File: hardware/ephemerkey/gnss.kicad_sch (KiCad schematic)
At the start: 0 parts

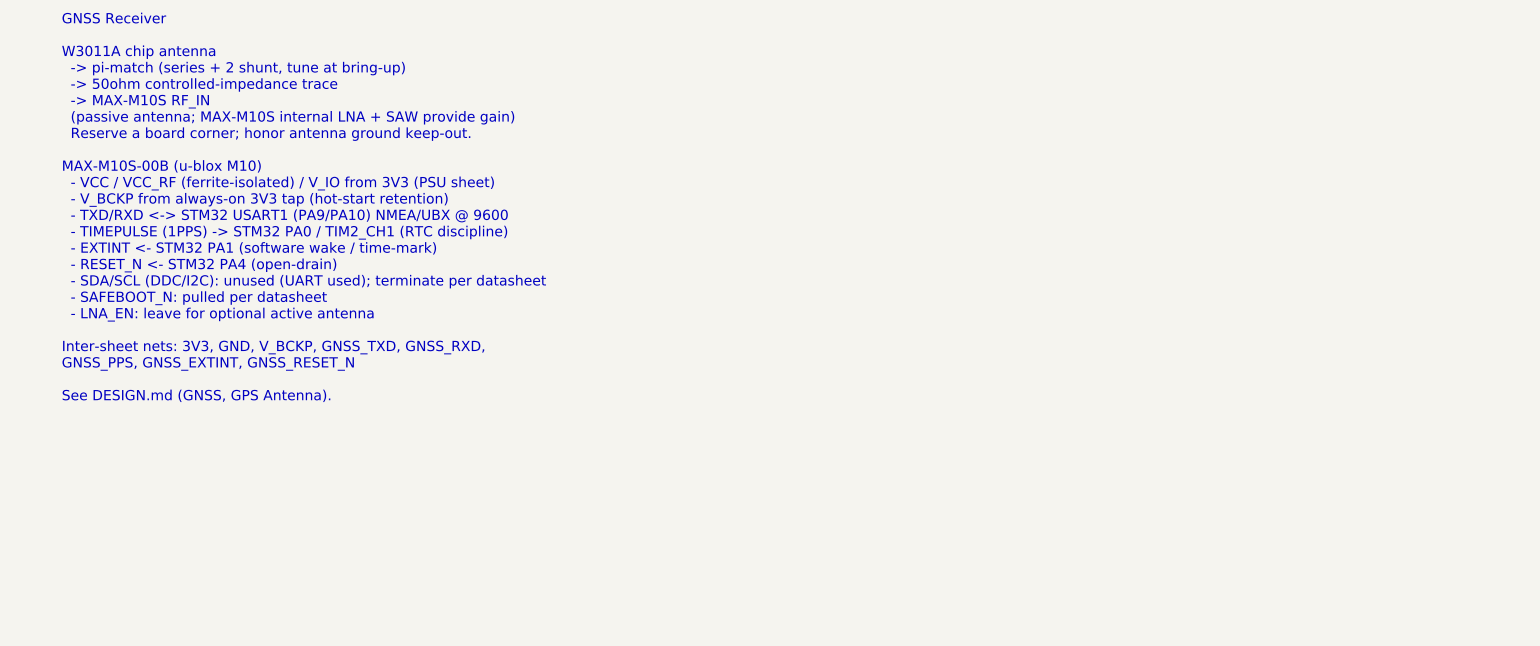
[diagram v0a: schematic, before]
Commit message: Populate schematic sheets per subsystem (placed, not wired)
Adopt the house schgen workflow (kschgen.py + manifest), matching notchdeck/
tsumikoro: schematic is GENERATED from scripts/ephemerkey.schgen.py, parts
PLACED with per-sheet on-canvas wiring notes; wiring is the next eeschema phase.

57 components across MCU / PSU / GNSS / Sensors, every line on a real KiCad
bundled symbol+footprint and a JLCPCB LCSC (0402 passives, 0805 bulk):
- MCU: STM32U083KCU6, 32.768kHz LSE crystal (C32346) + 12pF loads, SWD TC2030,
  lock-out header, decoupling, BOOT0/NRST, button, status LEDs.
- PSU: USB-C (GCT USB4105) + USBLC6 ESD + 5.1k CC, MCP73831 charger (Rprog 4.7k
  ~213mA for 500mAh), AO3401A load-share + B5819W, TPS63900 + FNR3015 2.2µH
  (small) + 10µF caps, JST-PH RA battery (S2B-PH-K-S).
- GNSS: MAX-M10S + W3011A + pi-match (series 0R, shunts DNP), VCC_RF ferrite,
  V_BCKP/V_IO/VCC decoupling.
- Sensors: LIS3DH + decoupling + 4.7k I2C pull-ups.

Tooling: kschgen.py, kicad-sch-check.py, kicad-sch-render.sh; Makefile gen/
check/render targets. make check: 57 comps, 57/57 footprints, no dup refs.
Added hardware/PARTS.md (BOM source of truth). CLAUDE.md documents the workflow.

Co-Authored-By: Claude Opus 4.8 (1M context) <noreply@anthropic.com>
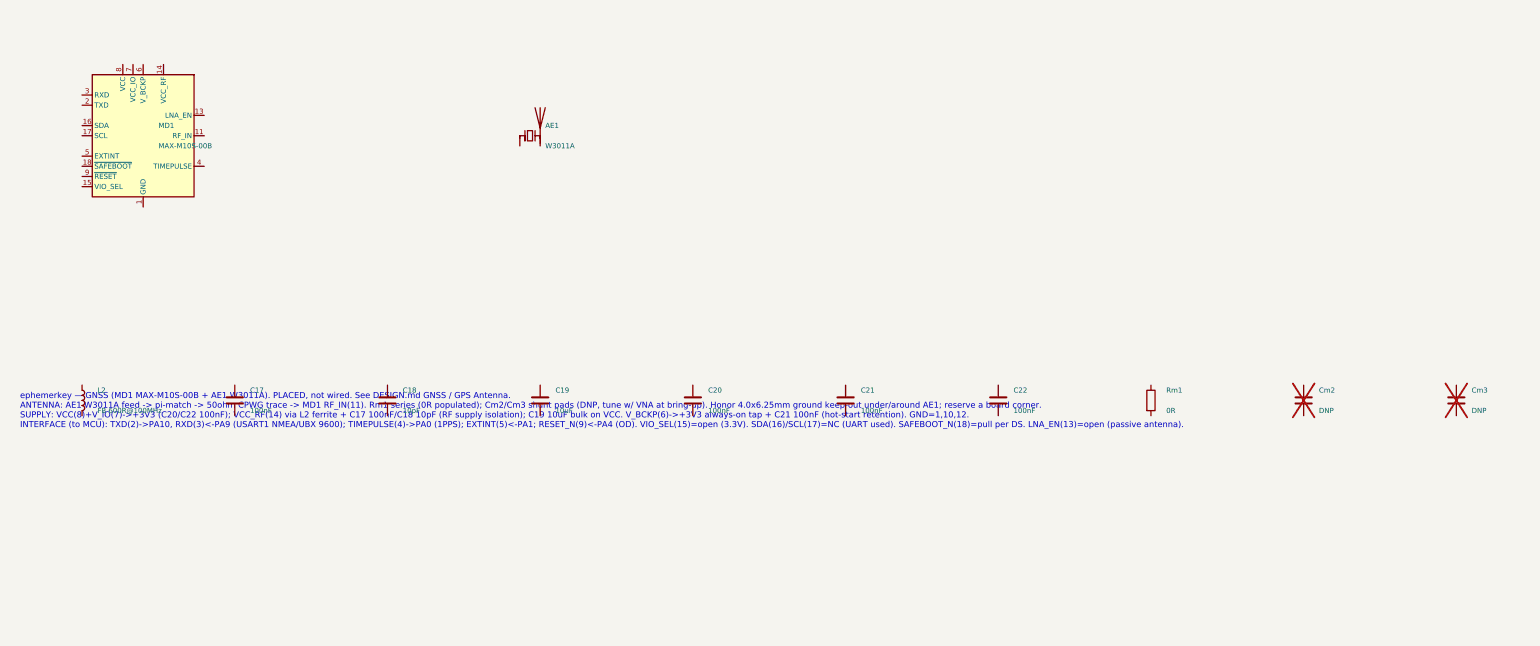
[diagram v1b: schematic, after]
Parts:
- added AE1: W3011A, RF_Antenna:Pulse_W3011, symbol Device:Antenna_Chip
- added C17, C20, C21, C22: 100nF, Capacitor_SMD:C_0402_1005Metric, symbol Device:C
- added C18: 10pF, Capacitor_SMD:C_0402_1005Metric, symbol Device:C
- added C19: 10uF, Capacitor_SMD:C_0805_2012Metric, symbol Device:C
- added Cm2, Cm3: DNP, Capacitor_SMD:C_0402_1005Metric, symbol Device:C
- added L2: FB 600R@100MHz, Inductor_SMD:L_0402_1005Metric, symbol Device:L
- added MD1: MAX-M10S-00B, RF_GPS:ublox_MAX, symbol RF_GPS:MAX-M10S
- added Rm1: 0R, Resistor_SMD:R_0402_1005Metric, symbol Device:R
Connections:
- new net: MD1.1 (GND), MD1.10 (GND), MD1.12 (GND)
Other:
- note added: "ephemerkey — GNSS (MD1 MAX-M10S-00B + AE1 W3011A). PLACED, not wired. See DESIGN.md GNSS / GPS Antenna. ANTENNA: AE1 W3011A feed -> pi-match -> 50ohm CPWG trace -> MD1 RF_IN(11). Rm1 series (0R populated); Cm2/Cm3 shunt pads (DNP, tune w/ VNA at bring-up). Honor 4.0x6.25mm ground keep-out under/around AE1; reserve a board corner. SUPPLY: VCC(8)+V_IO(7)->+3V3 (C20/C22 100nF); VCC_RF(14) via L2 fer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"
- note removed: "GNSS Receiver W3011A chip antenna -> pi-match (series + 2 shunt, tune at bring-up) -> 50ohm controlled-impedance trace -> MAX-M10S RF_IN (passive antenna; MAX-M10S internal LNA + SAW provide gain) Reserve a board corner; honor antenna ground keep-out. MAX-M10S-00B (u-blox M10) - VCC / VCC_RF (ferrite-isolated) / V_IO from 3V3 (PSU sheet) - V_BCKP from always-on 3V3 tap (hot-start retention) - TXD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"
- company: (none) -> EphemerKey Authors
- title: ephemerkey — GNSS -> ephemerkey — GNSS (MAX-M10S + antenna)

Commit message: Pinout-guide notes; vendor MAX + switch 3D models; 3 user buttons + DFU
Wiring notes: rewrote the four sheet notes from run-on prose into per-pin
PINOUT GUIDES (pin → net/function tables) per request.

3D models:
- MAX-M10S: vendored ublox_MAX-M10S.step (u-blox MAX form-factor, AP214, from
  fcmadwar/3D-Step-Models-Library) + project footprint ephemerkey:ublox_MAX
  with (model) repointed. Verify offset/rotation in 3D viewer.
- Switches: reuse tsumikoro's vendored ephemerkey:SW_Push_1P1T_XKB_TS-1187A
  footprint + STEP (the XKB TS-1187A model isn't in this KiCad bundle).
- Remaining to download: STM32U083 (UFQFPN-32), W3011A.

Switches: 3 user buttons (SW1→PA5, SW2→PA15 active-low; SW3→PF3/BOOT0
active-high). Holding SW3 at reset enters the STM32U0 ROM bootloader → USB DFU
over USB-C (confirmed in AN2606; crystal-less USB via HSI48+CRS).

make check: 59 components, 59/59 footprints, no dup refs. DESIGN.md pin budget +
library map, PARTS.md, 3dmodels README updated.

Co-Authored-By: Claude Opus 4.8 (1M context) <noreply@anthropic.com>
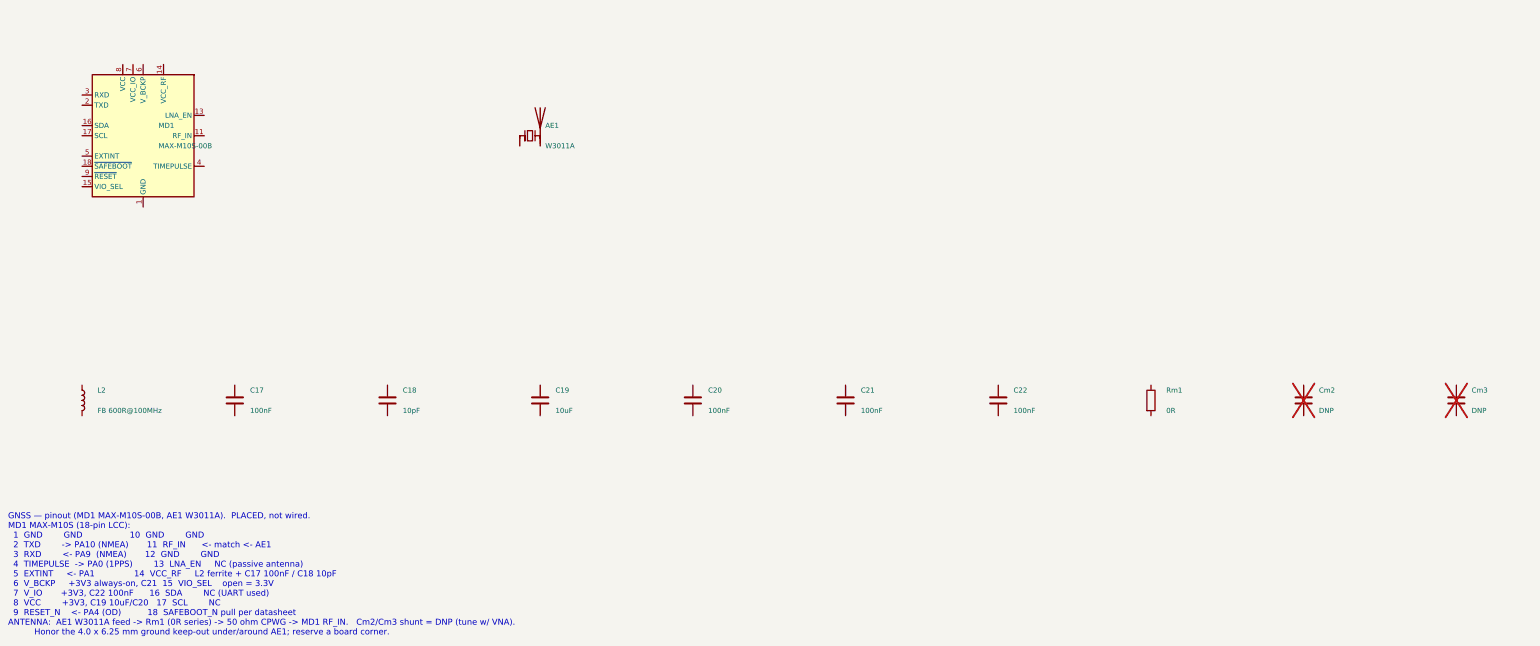
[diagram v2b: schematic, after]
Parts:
- MD1: footprint RF_GPS:ublox_MAX -> ephemerkey:ublox_MAX
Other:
- note added: "GNSS — pinout (MD1 MAX-M10S-00B, AE1 W3011A). PLACED, not wired. MD1 MAX-M10S (18-pin LCC): 1 GND GND 10 GND GND 2 TXD -> PA10 (NMEA) 11 RF_IN <- match <- AE1 3 RXD <- PA9 (NMEA) 12 GND GND 4 TIMEPULSE -> PA0 (1PPS) 13 LNA_EN NC (passive antenna) 5 EXTINT <- PA1 14 VCC_RF L2 ferrite + C17 100nF / C18 10pF 6 V_BCKP +3V3 always-on, C21 15 VIO_SEL open = 3.3V 7 V_IO +3V3, C22 100nF 16 SDA NC (UART u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"
- note removed: "ephemerkey — GNSS (MD1 MAX-M10S-00B + AE1 W3011A). PLACED, not wired. See DESIGN.md GNSS / GPS Antenna. ANTENNA: AE1 W3011A feed -> pi-match -> 50ohm CPWG trace -> MD1 RF_IN(11). Rm1 series (0R populated); Cm2/Cm3 shunt pads (DNP, tune w/ VNA at bring-up). Honor 4.0x6.25mm ground keep-out under/around AE1; reserve a board corner. SUPPLY: VCC(8)+V_IO(7)->+3V3 (C20/C22 100nF); VCC_RF(14) via L2 fer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"
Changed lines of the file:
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@@
 			(effects (font (size 1.27 1.27)) (justify left))
 		)
-		(property "Footprint" "RF_GPS:ublox_MAX"
+		(property "Footprint" "ephemerkey:ublox_MAX"
 			(at 45.7200 55.8800 0)
 			(effects (font (size 1.27 1.27))) (hide yes)
@@
 		(instances
 			(project "ephemerkey"
-				(path "/e1000000-0000-4000-8000-000000000001/c17334e3-27d7-4e80-b754-59599b68199a"
+				(path "/e1000000-0000-4000-8000-000000000001/bd4499f4-3240-4f39-b587-551f4e920631"
 					(reference "MD1")
 					(unit 1)
@@
 		(instances
 			(project "ephemerkey"
-				(path "/e1000000-0000-4000-8000-000000000001/c17334e3-27d7-4e80-b754-59599b68199a"
+				(path "/e1000000-0000-4000-8000-000000000001/bd4499f4-3240-4f39-b587-551f4e920631"
 					(reference "AE1")
 					(unit 1)
@@
 		(instances
 			(project "ephemerkey"
-				(path "/e1000000-0000-4000-8000-000000000001/c17334e3-27d7-4e80-b754-59599b68199a"
+				(path "/e1000000-0000-4000-8000-000000000001/bd4499f4-3240-4f39-b587-551f4e920631"
 					(reference "L2")
 					(unit 1)
@@
 		(instances
 			(project "ephemerkey"
-				(path "/e1000000-0000-4000-8000-000000000001/c17334e3-27d7-4e80-b754-59599b68199a"
+				(path "/e1000000-0000-4000-8000-000000000001/bd4499f4-3240-4f39-b587-551f4e920631"
 					(reference "C17")
 					(unit 1)
@@
 		(instances
 			(project "ephemerkey"
-				(path "/e1000000-0000-4000-8000-000000000001/c17334e3-27d7-4e80-b754-59599b68199a"
+				(path "/e1000000-0000-4000-8000-000000000001/bd4499f4-3240-4f39-b587-551f4e920631"
 					(reference "C18")
 					(unit 1)
@@
 		(instances
 			(project "ephemerkey"
-				(path "/e1000000-0000-4000-8000-000000000001/c17334e3-27d7-4e80-b754-59599b68199a"
+				(path "/e1000000-0000-4000-8000-000000000001/bd4499f4-3240-4f39-b587-551f4e920631"
 					(reference "C19")
 					(unit 1)
@@
 		(instances
 			(project "ephemerkey"
-				(path "/e1000000-0000-4000-8000-000000000001/c17334e3-27d7-4e80-b754-59599b68199a"
+				(path "/e1000000-0000-4000-8000-000000000001/bd4499f4-3240-4f39-b587-551f4e920631"
 					(reference "C20")
 					(unit 1)
@@
 		(instances
 			(project "ephemerkey"
-				(path "/e1000000-0000-4000-8000-000000000001/c17334e3-27d7-4e80-b754-59599b68199a"
+				(path "/e1000000-0000-4000-8000-000000000001/bd4499f4-3240-4f39-b587-551f4e920631"
 					(reference "C21")
 					(unit 1)
@@
 		(instances
 			(project "ephemerkey"
-				(path "/e1000000-0000-4000-8000-000000000001/c17334e3-27d7-4e80-b754-59599b68199a"
+				(path "/e1000000-0000-4000-8000-000000000001/bd4499f4-3240-4f39-b587-551f4e920631"
 					(reference "C22")
 					(unit 1)
@@
 		(instances
 			(project "ephemerkey"
-				(path "/e1000000-0000-4000-8000-000000000001/c17334e3-27d7-4e80-b754-59599b68199a"
+				(path "/e1000000-0000-4000-8000-000000000001/bd4499f4-3240-4f39-b587-551f4e920631"
 					(reference "Rm1")
 					(unit 1)
@@
 		(instances
 			(project "ephemerkey"
-				(path "/e1000000-0000-4000-8000-000000000001/c17334e3-27d7-4e80-b754-59599b68199a"
+				(path "/e1000000-0000-4000-8000-000000000001/bd4499f4-3240-4f39-b587-551f4e920631"
 					(reference "Cm2")
 					(unit 1)
@@
 		(instances
 			(project "ephemerkey"
-				(path "/e1000000-0000-4000-8000-000000000001/c17334e3-27d7-4e80-b754-59599b68199a"
+				(path "/e1000000-0000-4000-8000-000000000001/bd4499f4-3240-4f39-b587-551f4e920631"
 					(reference "Cm3")
 					(unit 1)
@@
 		)
 	)
-	(text "ephemerkey — GNSS (MD1 MAX-M10S-00B + AE1 W3011A). PLACED, not wired. See DESIGN.md GNSS / GPS Antenna.\nANTENNA: AE1 W3011A feed -> pi-match -> 50ohm CPWG trace -> MD1 RF_IN(11). Rm1 series (0R populated); Cm2/Cm3 shunt pads (DNP, tune w/ VNA at bring-up). Honor 4.0x6.25mm ground keep-out under/around AE1; reserve a board corner.\nSUPPLY: VCC(8)+V_IO(7)->+3V3 (C20/C22 100nF); VCC_RF(14) via L2 ferrite + C17 100nF/C18 10pF (RF supply isolation); C19 10uF bulk on VCC. V_BCKP(6)->+3V3 always-on tap + C21 100nF (hot-start retention). GND=1,10,12.\nINTERFACE (to MCU): TXD(2)->PA10, RXD(3)<-PA9 (USART1 NMEA/UBX 9600); TIMEPULSE(4)->PA0 (1PPS); EXTINT(5)<-PA1; RESET_N(9)<-PA4 (OD). VIO_SEL(15)=open (3.3V). SDA(16)/SCL(17)=NC (UART used). SAFEBOOT_N(18)=pull per DS. LNA_EN(13)=open (passive antenna)."
-		(exclude_from_sim no)
-		(at 15.00 120.00 0)
+	(text "GNSS — pinout (MD1 MAX-M10S-00B, AE1 W3011A).  PLACED, not wired.\nMD1 MAX-M10S (18-pin LCC):\n  1  GND        GND                  10  GND        GND\n  2  TXD        -> PA10 (NMEA)       11  RF_IN      <- match <- AE1\n  3  RXD        <- PA9  (NMEA)       12  GND        GND\n  4  TIMEPULSE  -> PA0 (1PPS)        13  LNA_EN     NC (passive antenna)\n  5  EXTINT     <- PA1               14  VCC_RF     L2 ferrite + C17 100nF / C18 10pF\n  6  V_BCKP     +3V3 always-on, C21  15  VIO_SEL    open = 3.3V\n  7  V_IO       +3V3, C22 100nF      16  SDA        NC (UART used)\n  8  VCC        +3V3, C19 10uF/C20   17  SCL        NC\n  9  RESET_N    <- PA4 (OD)          18  SAFEBOOT_N pull per datasheet\nANTENNA:  AE1 W3011A feed -> Rm1 (0R series) -> 50 ohm CPWG -> MD1 RF_IN.   Cm2/Cm3 shunt = DNP (tune w/ VNA).\n          Honor the 4.0 x 6.25 mm ground keep-out under/around AE1; reserve a board corner."
+		(exclude_from_sim no)
+		(at 12.00 150.00 0)
 		(effects (font (size 1.5 1.5)) (justify left top))
 	)
